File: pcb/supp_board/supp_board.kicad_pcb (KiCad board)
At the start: 2 copper layers, 69 x 70 mm, 24 parts, among them J10 Screw_Terminal_01x03, J2 Conn_01x02_Pin, J3 Screw_Terminal_01x04, J4 Screw_Terminal_01x04, J5 Screw_Terminal_01x04, J6 Conn_01x08_Socket, J7 Conn_01x08_Socket, J8 Conn_01x08_Socket, J9 Conn_01x08_Socket, Q1 IRLZ44N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

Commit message: Add work from 2025-07-27
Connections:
- J9 pad 2: unconnected-(J9-Pin_2-Pad2) -> GND
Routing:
- net GND: track 251.3 -> 282.4 mm

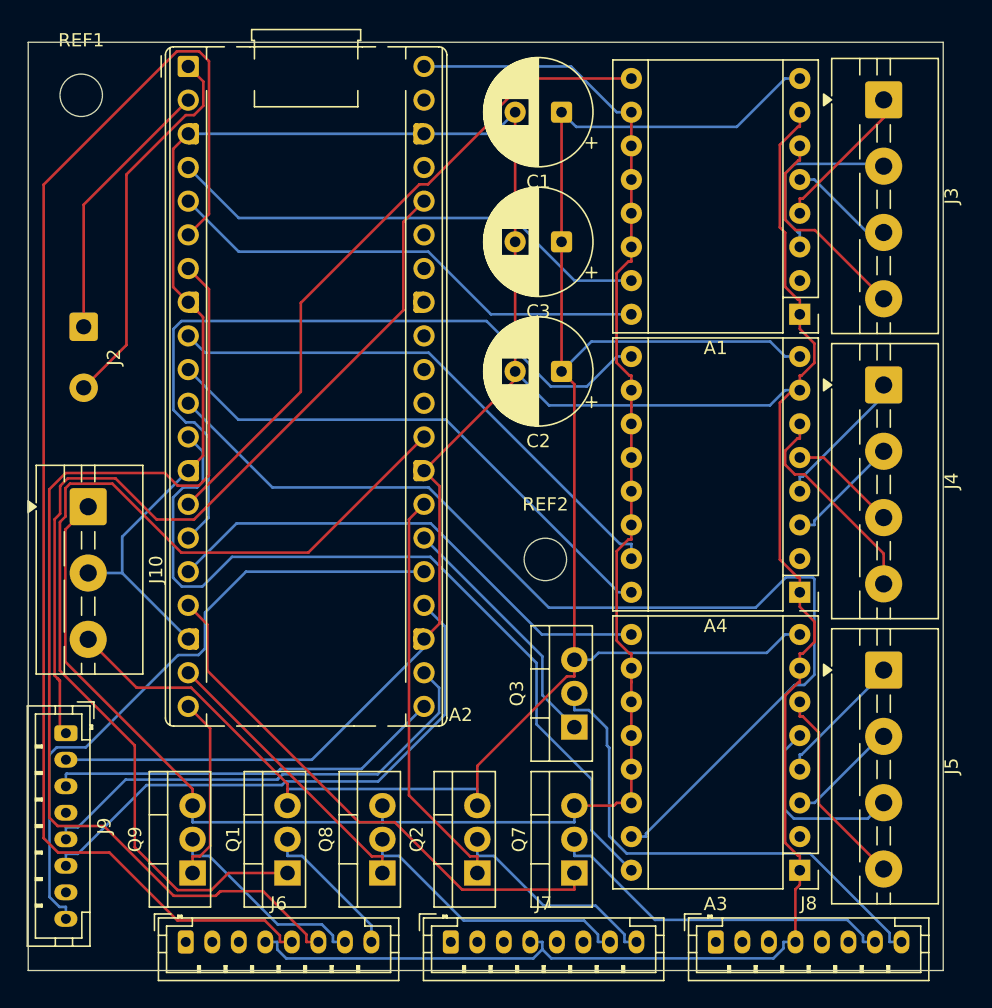
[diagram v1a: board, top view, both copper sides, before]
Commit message: Reroute supp. board
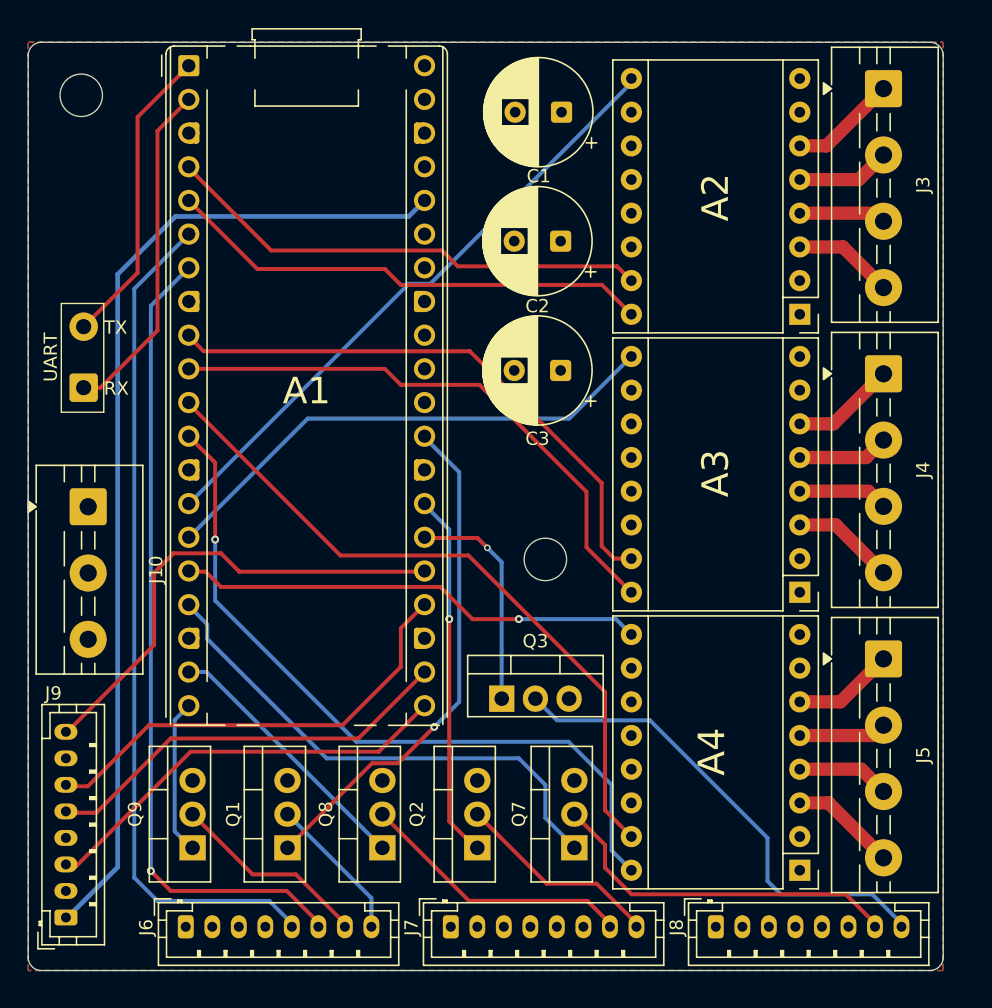
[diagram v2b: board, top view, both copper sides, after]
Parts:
- A1: renamed from A2; footprint Module:RaspberryPi_Pico_Common_THT -> PiPico:Untitled
- moved A1 25.7 mm to (53.5, 69.4)
- moved J9 13.9 mm to (35.3, 109.5), turned to 90 degrees
- moved C2 9.83 mm to (72.7, 58.5)
- moved C3 9.70 mm to (72.7, 68.2)
- moved Q3 5.88 mm to (68.2, 93.0), turned to 0 degrees
- moved UART 4.59 mm to (36.7, 69.5), turned to 90 degrees
- moved Q1 1.89 mm to (52.1, 104.2)
- moved Q2 1.89 mm to (66.4, 104.2)
- moved Q7 1.89 mm to (73.7, 104.2)
- moved Q8 1.89 mm to (59.2, 104.2)
- moved Q9 1.89 mm to (44.9, 104.2)
- moved J6 1.14 mm to (44.4, 110.2)
- moved J7 1.14 mm to (64.4, 110.2)
- moved J8 1.14 mm to (84.4, 110.2)
- moved J3 0.85 mm to (97.0, 47.0)
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- renumbered A1 to A2, A4 to A3, A3 to A4, J2 to UART
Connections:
- A2 pad 3: Net-(A1-A2) -> Net-(A2-A2)
- A2 pad 4: Net-(A1-A1) -> Net-(A2-A1)
- A2 pad 5: Net-(A1-B1) -> Net-(A2-B1)
- A2 pad 6: Net-(A1-B2) -> Net-(A2-B2)
- A3 pad 3: Net-(A4-A2) -> Net-(A3-A2)
- A3 pad 4: Net-(A4-A1) -> Net-(A3-A1)
- A3 pad 5: Net-(A4-B1) -> Net-(A3-B1)
- A3 pad 6: Net-(A4-B2) -> Net-(A3-B2)
- A4 pad 3: Net-(A3-A2) -> Net-(A4-A2)
- A4 pad 4: Net-(A3-A1) -> Net-(A4-A1)
- A4 pad 5: Net-(A3-B1) -> Net-(A4-B1)
- A4 pad 6: Net-(A3-B2) -> Net-(A4-B2)
- J3 pad 1: Net-(A1-A1) -> Net-(A2-B2)
- J3 pad 2: Net-(A1-A2) -> Net-(A2-B1)
- J3 pad 3: Net-(A1-B1) -> Net-(A2-A1)
- J3 pad 4: Net-(A1-B2) -> Net-(A2-A2)
- J4 pad 1: Net-(A4-A1) -> Net-(A3-B2)
- J4 pad 2: Net-(A4-A2) -> Net-(A3-B1)
- J4 pad 3: Net-(A4-B1) -> Net-(A3-A1)
- J4 pad 4: Net-(A4-B2) -> Net-(A3-A2)
- J5 pad 1: Net-(A3-A1) -> Net-(A4-B2)
- J5 pad 2: Net-(A3-A2) -> Net-(A4-B1)
- J5 pad 3: Net-(A3-B1) -> Net-(A4-A1)
- J5 pad 4: Net-(A3-B2) -> Net-(A4-A2)
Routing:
- net GND: track 282.4 -> 0.00 mm
- net /+24V: track 151.1 -> 0.00 mm
- net /+5V: track 135.6 -> 0.00 mm
- net /TPLG_TX: track 102.2 -> 63.5 mm
- net Net-(A1-GPIO22): track 75.9 -> 38.6 mm, vias 0 -> 1
- net Net-(A1-GPIO8): track 80.8 -> 52.2 mm
- net /TPLG_RX: track 79.3 -> 60.8 mm, vias 0 -> 1
- net Net-(A1-GPIO11): track 55.7 -> 39.1 mm
- net Net-(A1-B2): track 16.0 -> 0.00 mm
- net Net-(A1-A2): track 13.9 -> 0.00 mm
- net Net-(A1-3V3): track 62.2 -> 75.6 mm
- net Net-(A1-GPIO19): track 48.7 -> 36.4 mm
- net Net-(A1-A1): track 11.3 -> 0.00 mm
- net Net-(A4-B2): track 16.1 -> 7.66 mm
- net Net-(A1-GPIO18): track 42.7 -> 34.4 mm
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- added copper zone on In1.Cu, net /+24V
- added copper zone on In2.Cu, net /+5V
- added copper zone on B.Cu, net GND
- added copper zone on F.Cu, net GND
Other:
- outline, holes or cut-outs redrawn
- copper layers 2 -> 4
- board text added: "RX"
- board text added: "TX"

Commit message: Replace boykissers on PCBs with my pfp (copyright reasons :3)
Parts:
- added G***: LOGO, LOGO, F.Cu at (37.8, 52.5)
- added G***: LOGO, LOGO, B.Cu at (84.5, 50.5)
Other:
- board text added: "xt-1 0.0.0-proto redbigz.com"
- board text added: "xt-1 0.0.0-proto supplementary motherboard v2 by redbigz"
